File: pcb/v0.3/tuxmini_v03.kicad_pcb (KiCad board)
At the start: 2 copper layers, 32 x 32 mm, 82 parts, among them J1 USB_C_Receptacle_USB2.0_16P, J3 Conn_01x09, J4 Conn_01x10, J6 Conn_01x02, J7 Conn_01x02, J8 Conn_01x03, Q1 DMG1045U, Q2 Si2301CDS, Q3 2N7002, SW1 Boot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

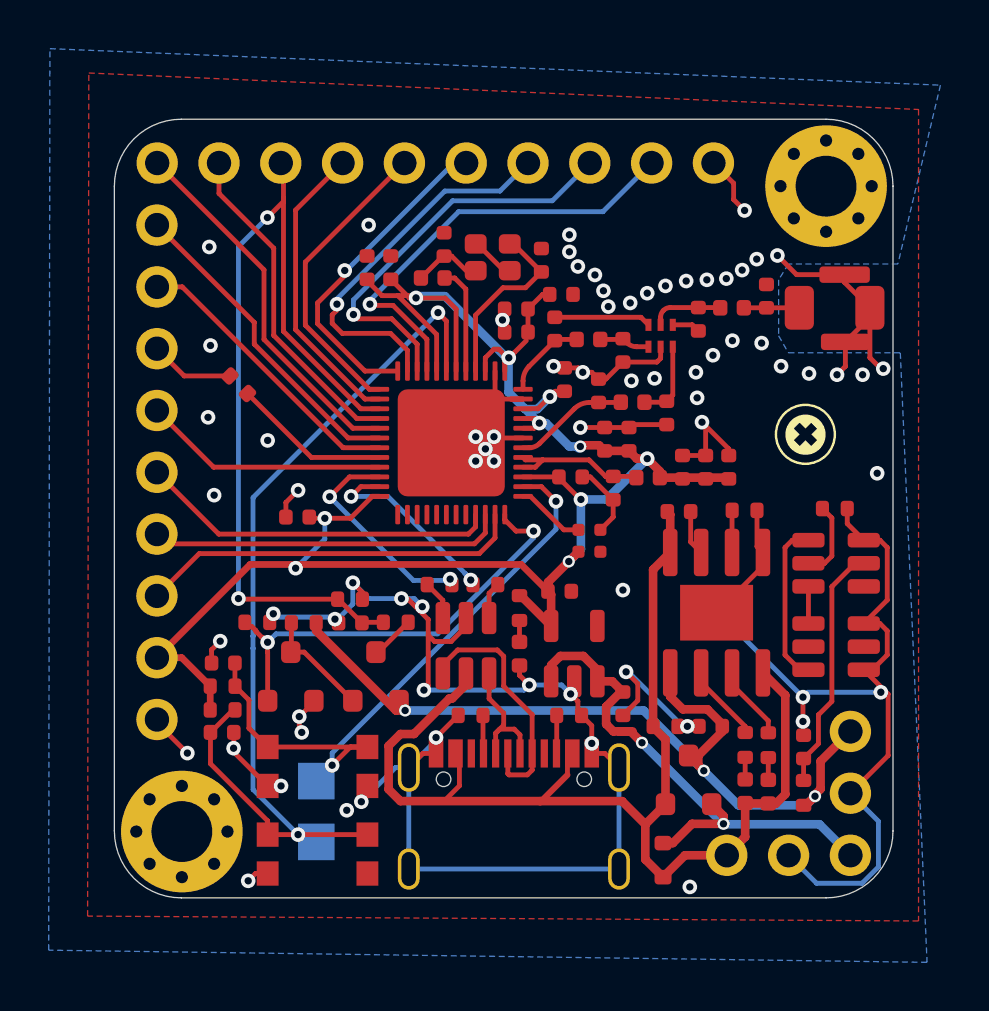
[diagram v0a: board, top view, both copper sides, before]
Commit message: Swaped D- and D+ pin on ESP32-C5 pinout
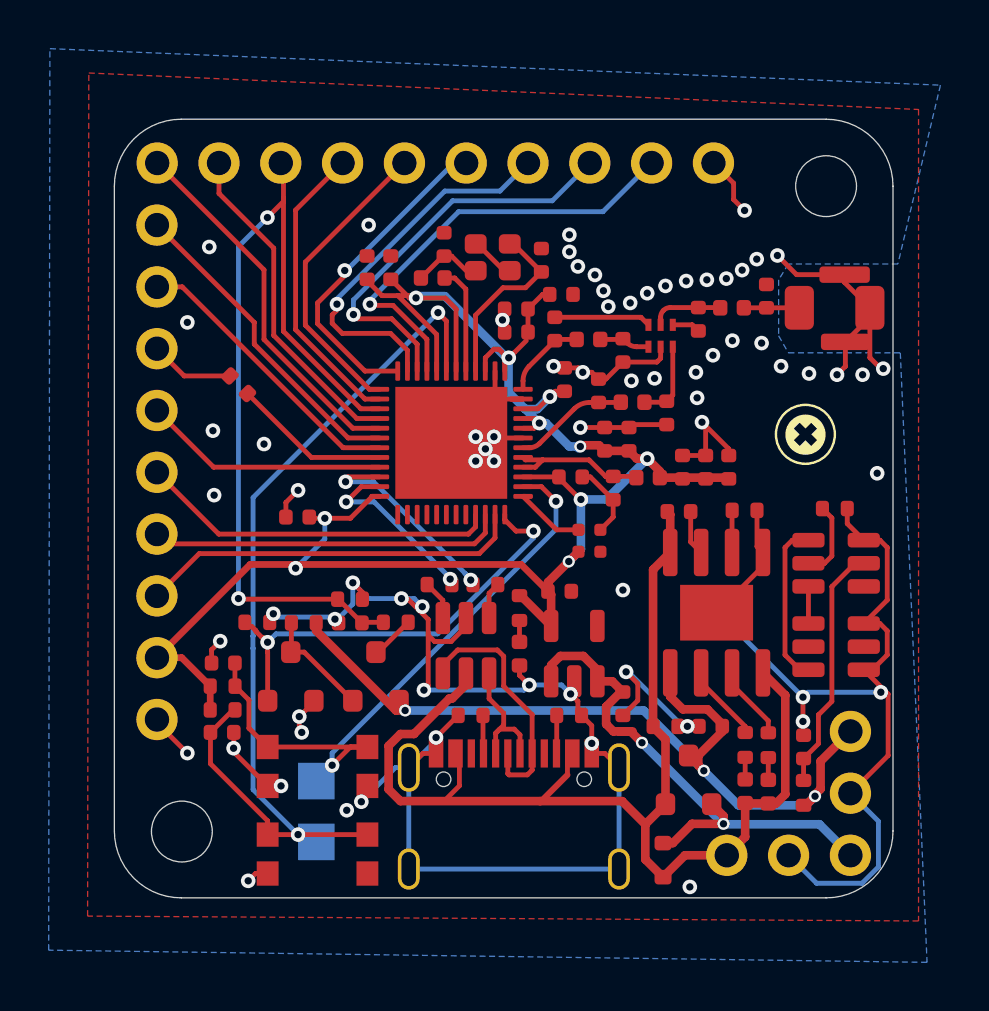
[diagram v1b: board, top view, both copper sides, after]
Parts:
- added REF**: Logo, BRC1518:Logo, B.Cu at (146.8, 81.3)
- moved REF** 13.9 mm to (132.4, 72.7)
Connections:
- U1 pad 22: D+ -> D-
- U1 pad 23: D- -> D+
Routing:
- net D+: track 8.98 -> 7.50 mm
- net D-: track 8.30 -> 8.98 mm
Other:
- board text added: "ADC: SCK: MISO: MOSI:"
- board text added: "CH000029"
- board text added: "ESP32-C5 Tux Board by lifex"
- board text added: "IO1-IO6 IO8 IO9 IO10"
- board text added: "IO11 TX"
- board text added: "IO12 RX"
- board text added: "IO23 SDA"
- board text added: "IO24 SCL"
- board text added: "Licensed under CERN-OHL-S v2"
- board text removed: "ESP32-C5 Tux Board by lifex Licensed under CERN-OHL-S v2"
- board text removed: "RX"
- board text removed: "SCL"
- board text removed: "SDA"
- board text removed: "TX"
